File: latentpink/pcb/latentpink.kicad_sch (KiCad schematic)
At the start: 32 parts, among them M10 WEEE, M3 SCREWHOLE, M4 SCREWHOLE, M5 SCREWHOLE, M6 SCREWHOLE, M7 LONGTHING, M8 OSHW, M9 POLARITY, U36 AT30TS74_UDFN, U37 AT30TS74_UDFN, U38 AT30TS74_UDFN, U39 AT30TS74_UDFN

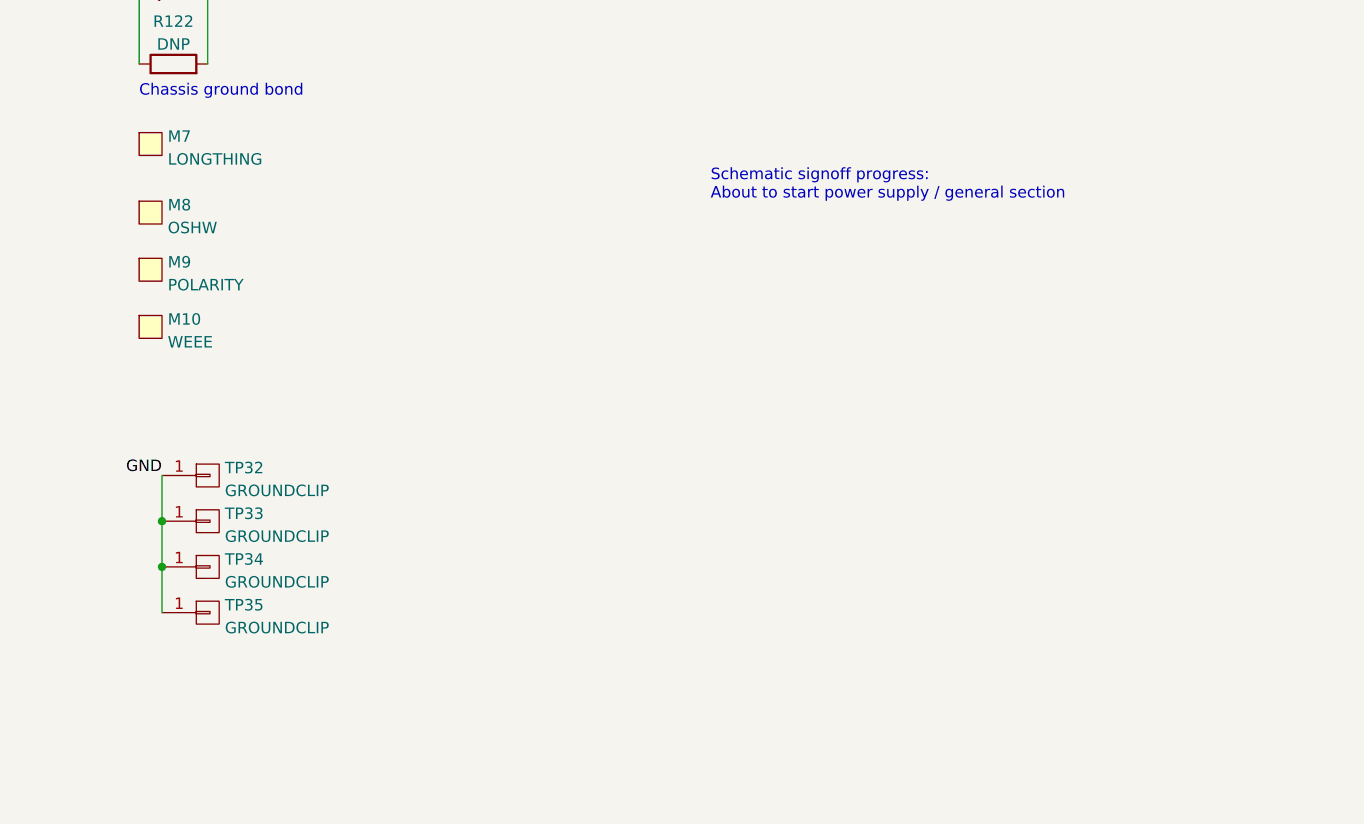
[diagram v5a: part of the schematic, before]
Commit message: Finished initial schematic review, added ESD diodes to Ethernet pairs
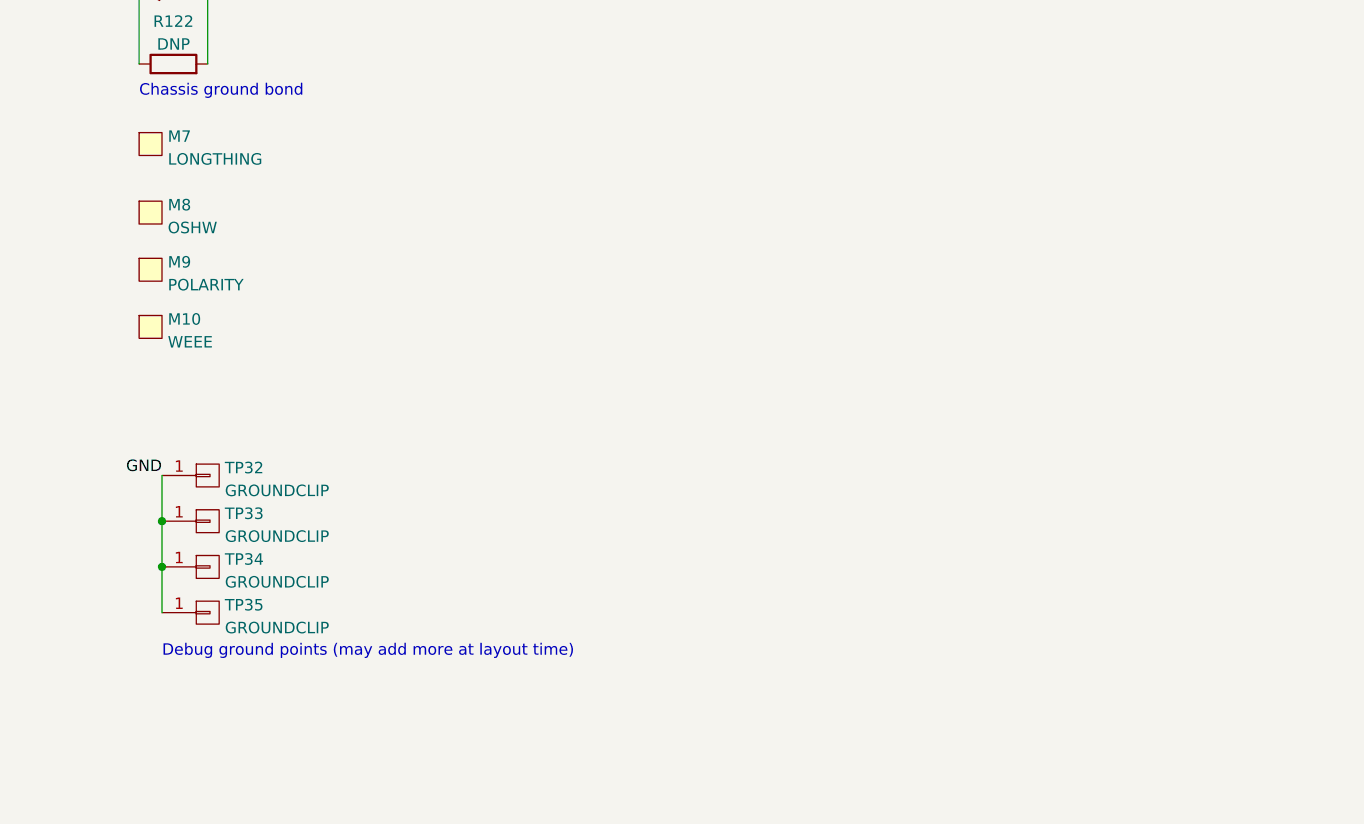
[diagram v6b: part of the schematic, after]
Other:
- note added: "Debug ground points (may add more at layout time)"
- note removed: "Schematic signoff progress: About to start power supply / general section"
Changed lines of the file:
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@@
     (stroke (width 0) (type default) (color 0 0 0 0))
   )
-  (text "Schematic signoff progress:\nAbout to start power supply / general section"
-    (at 133.35 133.35 0)
-    (effects (font (size 1.27 1.27)) (justify left bottom))
-  )
   (text "Address = 8'h90" (at 298.45 36.83 0)
     (effects (font (size 1.27 1.27)) (justify left bottom))
@@
     (effects (font (size 1.27 1.27)) (justify left bottom))
   )
+  (text "Debug ground points (may add more at layout time)" (at 72.39 184.15 0)
+    (effects (font (size 1.27 1.27)) (justify left bottom))
+  )
   (label "3V3" (at 295.91 83.82 180)
     (effects (font (size 1.27 1.27)) (justify right bottom))
@@
     )
     (path "/70fb61fd-2f76-4850-9d6b-7e1d9a86570a/78eecf8b-2789-4144-a6b7-458d044a281a"
-      (reference "R14") (unit 1) (value "10K") (footprint "azonenberg_pcb:EIA_0402_RES_NOSILK")
+      (reference "R14") (unit 1) (value "DNP") (footprint "azonenberg_pcb:EIA_0402_RES_NOSILK")
     )
     (path "/70fb61fd-2f76-4850-9d6b-7e1d9a86570a/5ec38d89-6595-48ed-8d79-f385cb86a61d"
@@
       (reference "U39") (unit 1) (value "AT30TS74_UDFN") (footprint "azonenberg_pcb:DFN_8_0.5MM_2x3MM_TALL")
     )
+    (path "/d0e7363b-23d9-4272-a4d1-0db2834b87f3/3f704481-088c-47de-abc3-38e6895ce91f"
+      (reference "U40") (unit 1) (value "RCLAMP0514M") (footprint "azonenberg_pcb:SOP_10_0.5MM_3MM")
+    )
+    (path "/d0e7363b-23d9-4272-a4d1-0db2834b87f3/1b07a677-26b0-449d-8070-83ecf83a62b5"
+      (reference "U41") (unit 1) (value "RCLAMP0514M") (footprint "azonenberg_pcb:SOP_10_0.5MM_3MM")
+    )
+    (path "/d0e7363b-23d9-4272-a4d1-0db2834b87f3/7f603147-0502-4caf-92be-b1b6a471faa1"
+      (reference "U42") (unit 1) (value "RCLAMP0514M") (footprint "azonenberg_pcb:SOP_10_0.5MM_3MM")
+    )
+    (path "/d0e7363b-23d9-4272-a4d1-0db2834b87f3/4313a044-81fe-4936-935b-77af07209a24"
+      (reference "U43") (unit 1) (value "RCLAMP0514M") (footprint "azonenberg_pcb:SOP_10_0.5MM_3MM")
+    )
+    (path "/d0e7363b-23d9-4272-a4d1-0db2834b87f3/3a12eab6-ee93-4b0e-9f03-59b75cad863f"
+      (reference "U44") (unit 1) (value "RCLAMP0514M") (footprint "azonenberg_pcb:SOP_10_0.5MM_3MM")
+    )
+    (path "/d0e7363b-23d9-4272-a4d1-0db2834b87f3/cbf48daf-9a5c-4c50-b788-025e94475671"
+      (reference "U45") (unit 1) (value "RCLAMP0514M") (footprint "azonenberg_pcb:SOP_10_0.5MM_3MM")
+    )
+    (path "/d0e7363b-23d9-4272-a4d1-0db2834b87f3/75ae1b41-cd85-4f67-abd2-74ca2087b945"
+      (reference "U46") (unit 1) (value "RCLAMP0514M") (footprint "azonenberg_pcb:SOP_10_0.5MM_3MM")
+    )
+    (path "/d0e7363b-23d9-4272-a4d1-0db2834b87f3/ded72b3d-ca3b-4833-8c55-1c5300a0e1b4"
+      (reference "U47") (unit 1) (value "RCLAMP0514M") (footprint "azonenberg_pcb:SOP_10_0.5MM_3MM")
+    )
+    (path "/d0e7363b-23d9-4272-a4d1-0db2834b87f3/fcad12aa-0765-4007-a275-6c513f12ec66"
+      (reference "U48") (unit 1) (value "RCLAMP0514M") (footprint "azonenberg_pcb:SOP_10_0.5MM_3MM")
+    )
+    (path "/d0e7363b-23d9-4272-a4d1-0db2834b87f3/42e79451-2219-4b18-a479-6e44450bf4f6"
+      (reference "U49") (unit 1) (value "RCLAMP0514M") (footprint "azonenberg_pcb:SOP_10_0.5MM_3MM")
+    )
+    (path "/d0e7363b-23d9-4272-a4d1-0db2834b87f3/052b9873-a982-4227-848c-10158c78aee0"
+      (reference "U50") (unit 1) (value "RCLAMP0514M") (footprint "azonenberg_pcb:SOP_10_0.5MM_3MM")
+    )
+    (path "/d0e7363b-23d9-4272-a4d1-0db2834b87f3/6af7e5e2-246e-476a-9f74-d63ccca8b32b"
+      (reference "U51") (unit 1) (value "RCLAMP0514M") (footprint "azonenberg_pcb:SOP_10_0.5MM_3MM")
+    )
+    (path "/d0e7363b-23d9-4272-a4d1-0db2834b87f3/219b6a96-df34-4479-a274-6416406bfab9"
+      (reference "U52") (unit 1) (value "RCLAMP0514M") (footprint "azonenberg_pcb:SOP_10_0.5MM_3MM")
+    )
+    (path "/d0e7363b-23d9-4272-a4d1-0db2834b87f3/52b7bf0e-044b-4e73-98ca-5dd669e82726"
+      (reference "U53") (unit 1) (value "RCLAMP0514M") (footprint "azonenberg_pcb:SOP_10_0.5MM_3MM")
+    )
+    (path "/d0e7363b-23d9-4272-a4d1-0db2834b87f3/6d45e6ff-805b-4288-b6cc-c92ec9fc6551"
+      (reference "U54") (unit 1) (value "RCLAMP0514M") (footprint "azonenberg_pcb:SOP_10_0.5MM_3MM")
+    )
+    (path "/d0e7363b-23d9-4272-a4d1-0db2834b87f3/8c470854-0b0a-488b-82ba-ba3e2eb261de"
+      (reference "U55") (unit 1) (value "RCLAMP0514M") (footprint "azonenberg_pcb:SOP_10_0.5MM_3MM")
+    )
+    (path "/d0e7363b-23d9-4272-a4d1-0db2834b87f3/f2803b37-9908-4144-b3f3-bbaf2a6d6940"
+      (reference "U56") (unit 1) (value "RCLAMP0514M") (footprint "azonenberg_pcb:SOP_10_0.5MM_3MM")
+    )
+    (path "/d0e7363b-23d9-4272-a4d1-0db2834b87f3/36a2c9e9-924c-4312-9713-4320c11e383b"
+      (reference "U57") (unit 1) (value "RCLAMP0514M") (footprint "azonenberg_pcb:SOP_10_0.5MM_3MM")
+    )
+    (path "/d0e7363b-23d9-4272-a4d1-0db2834b87f3/781c3da1-bb51-445b-979c-c867d809bd52"
+      (reference "U58") (unit 1) (value "RCLAMP0514M") (footprint "azonenberg_pcb:SOP_10_0.5MM_3MM")
+    )
+    (path "/d0e7363b-23d9-4272-a4d1-0db2834b87f3/dff6c742-0d8c-46e1-b811-978889075608"
+      (reference "U59") (unit 1) (value "RCLAMP0514M") (footprint "azonenberg_pcb:SOP_10_0.5MM_3MM")
+    )
+    (path "/d0e7363b-23d9-4272-a4d1-0db2834b87f3/c8fb365e-d863-4735-b58e-87894309034d"
+      (reference "U60") (unit 1) (value "RCLAMP0514M") (footprint "azonenberg_pcb:SOP_10_0.5MM_3MM")
+    )
+    (path "/d0e7363b-23d9-4272-a4d1-0db2834b87f3/a21fe9d8-002d-443c-a18b-b88c9a559d81"
+      (reference "U61") (unit 1) (value "RCLAMP0514M") (footprint "azonenberg_pcb:SOP_10_0.5MM_3MM")
+    )
+    (path "/d0e7363b-23d9-4272-a4d1-0db2834b87f3/053bb1b7-8f8a-4a7b-a53d-5fe80c9fd9f6"
+      (reference "U62") (unit 1) (value "RCLAMP0514M") (footprint "azonenberg_pcb:SOP_10_0.5MM_3MM")
+    )
+    (path "/d0e7363b-23d9-4272-a4d1-0db2834b87f3/0d6a1662-f085-4e28-bbab-24e2db022f80"
+      (reference "U63") (unit 1) (value "RCLAMP0514M") (footprint "azonenberg_pcb:SOP_10_0.5MM_3MM")
+    )
+    (path "/035a8a96-1dae-486c-a84e-a11c0c87b4ac/626b4a48-b66a-4c2b-9c82-5662baf5dfe0/a8eff87b-0b24-407d-ae30-084902115f59"
+      (reference "U64") (unit 1) (value "RCLAMP0514M") (footprint "azonenberg_pcb:SOP_10_0.5MM_3MM")
+    )
+    (path "/035a8a96-1dae-486c-a84e-a11c0c87b4ac/626b4a48-b66a-4c2b-9c82-5662baf5dfe0/a4fc545c-1018-46a8-b09c-57cd78b9392d"
+      (reference "U65") (unit 1) (value "RCLAMP0514M") (footprint "azonenberg_pcb:SOP_10_0.5MM_3MM")
+    )
   )

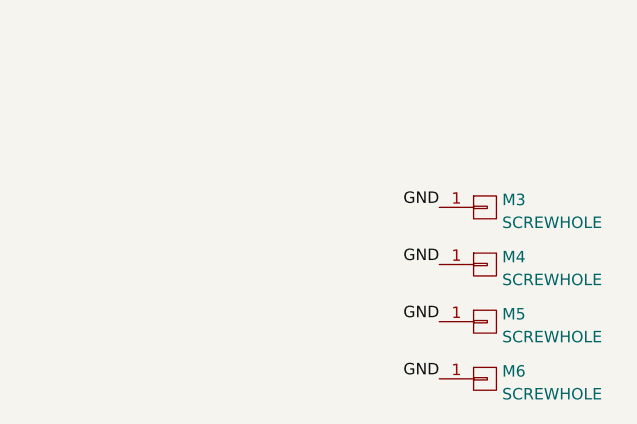
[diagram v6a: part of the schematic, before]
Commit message: Preliminary routing of first four baseT interfaces on VSC8512
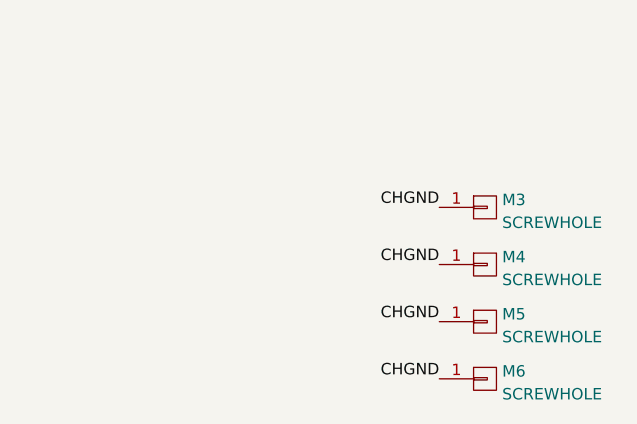
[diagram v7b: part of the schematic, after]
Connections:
- net CHGND: now also M3.1 (P1), M4.1 (P1), M5.1 (P1), M6.1 (P1)
- net GND: no longer M3.1 (P1), M4.1 (P1), M5.1 (P1), M6.1 (P1)
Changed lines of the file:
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@@
     (effects (font (size 1.27 1.27)) (justify left bottom))
   )
-  (label "GND" (at 365.76 224.79 180)
+  (label "CHGND" (at 365.76 224.79 180)
     (effects (font (size 1.27 1.27)) (justify right bottom))
   )
@@
     (effects (font (size 1.27 1.27)) (justify right bottom))
   )
-  (label "GND" (at 365.76 231.14 180)
+  (label "CHGND" (at 365.76 231.14 180)
     (effects (font (size 1.27 1.27)) (justify right bottom))
   )
@@
     (effects (font (size 1.27 1.27)) (justify right bottom))
   )
-  (label "GND" (at 365.76 237.49 180)
+  (label "CHGND" (at 365.76 237.49 180)
     (effects (font (size 1.27 1.27)) (justify right bottom))
   )
@@
     (effects (font (size 1.27 1.27)) (justify right bottom))
   )
-  (label "GND" (at 365.76 243.84 180)
+  (label "CHGND" (at 365.76 243.84 180)
     (effects (font (size 1.27 1.27)) (justify right bottom))
   )
